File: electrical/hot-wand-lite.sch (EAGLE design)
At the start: 77 parts, among them IC1 12V R-78K12-2.0, IC2 AMS1117-5.0, Q1 NCHAN, Q2 SIRS5800DP-T1-GE3, Q3 DMTH64M2LPDWQ-13, Q4 2N7002K, Q5 G3404, U1 SEEED-XIAO-SAMD21, U2 1EDN8511BXUSA1, U3 LM74700QDBVTQ1, U4 AP53781

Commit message: added a selector for ISEL
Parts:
- removed JP4: (no value), hot-wand:M03LOCK
- removed SJ2: SOLDERJUMPERNO, hot-wand:SOLDERJUMPERNO
- JP5: device hot-wand:M03LOCK -> hot-wand:M06LOCK; JLC-DNP 1 -> (none)
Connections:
- removed net N$55: R15.2, SJ2.1
- removed net N$9: JP5.1, R18.2
- removed net SWDIO: JP4.2, R7.1, R8.1
- new net FAN-CTRL: JP5.2, R7.1, R8.1
- new net USB-I-SEL: JP5.5, R15.2
- new net USB-V-SEL: JP5.3, R18.2
- net +12V: now also JP5.1; no longer JP4.3
- net GND: now also JP5.4, JP5.6; no longer JP4.1, JP5.2, JP5.3, SJ2.2
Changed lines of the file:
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@@
-<attribute name="JLC-DNP" value="1"/>
-</part>
-<part name="SJ2" library="hot-wand" deviceset="SOLDERJUMPER" device="NO" value="">
 <attribute name="JLC-DNP" value="1"/>
 </part>
@@
 </part>
 <part name="U$2" library="hot-wand" deviceset="5V" device=""/>
-<part name="P+2" library="hot-wand" deviceset="+12V" device=""/>
 <part name="GND8" library="hot-wand" deviceset="GND" device=""/>
-<part name="JP5" library="hot-wand" deviceset="M03" device="LOCK">
-<attribute name="JLC-DNP" value="1"/>
-</part>
-<part name="GND9" library="hot-wand" deviceset="GND" device=""/>
 <part name="R17" library="hot-wand" deviceset="RESISTOR" device="0603-RES" value="3K">
 <attribute name="JLCPARTNUM" value="C4211"/>
 </part>
-<part name="GND10" library="hot-wand" deviceset="GND" device=""/>
 <part name="JP6" library="hot-wand" deviceset="M04" device="LOCK">
-<attribute name="JLC-DNP" value="1"/>
-</part>
-<part name="JP4" library="hot-wand" deviceset="M03" device="LOCK">
 <attribute name="JLC-DNP" value="1"/>
 </part>
@@
 <attribute name="JLC-DNP" value="1"/>
 </part>
-<part name="GND12" library="hot-wand" deviceset="GND" device=""/>
 <part name="PCB2" library="hot-wand" deviceset="PCB-ART-VER-LITE" device="">
 <attribute name="DNP" value="1"/>
@@
 <attribute name="JLCPARTNUM" value="C23242"/>
 </part>
+<part name="JP5" library="hot-wand" deviceset="M06" device="LOCK"/>
 </parts>
 <sheets>
@@
 <attribute name="VALUE" x="148.59" y="-567.436" size="1.778" layer="96"/>
 </instance>
-<instance part="SJ2" gate="1" x="165.1" y="-568.96"/>
 <instance part="R13" gate="G$1" x="157.48" y="-538.48" smashed="yes" rot="R270">
 <attribute name="NAME" x="153.8986" y="-534.67" size="1.778" layer="95" rot="R270"/>
@@
 </instance>
 <instance part="U$2" gate="G$1" x="109.22" y="-312.42"/>
-<instance part="P+2" gate="1" x="167.64" y="-398.78"/>
 <instance part="GND8" gate="1" x="109.22" y="-345.44"/>
-<instance part="JP5" gate="G$1" x="187.96" y="-609.6" rot="R180">
-<attribute name="JLC-DNP" x="187.96" y="-609.6" size="1.778" layer="96" rot="R180" display="off"/>
-</instance>
-<instance part="GND9" gate="1" x="172.72" y="-574.04"/>
 <instance part="R17" gate="G$1" x="172.72" y="-586.74" smashed="yes" rot="R270">
 <attribute name="NAME" x="169.1386" y="-582.93" size="1.778" layer="95" rot="R270"/>
@@
 <attribute name="JLCPARTNUM" x="172.72" y="-586.74" size="1.778" layer="96" rot="R270" display="off"/>
 </instance>
-<instance part="GND10" gate="1" x="177.8" y="-617.22"/>
 <instance part="JP6" gate="G$1" x="144.78" y="-317.5" rot="R180">
 <attribute name="JLC-DNP" x="144.78" y="-317.5" size="1.778" layer="96" rot="R180" display="off"/>
-</instance>
-<instance part="JP4" gate="G$1" x="147.32" y="-408.94">
-<attribute name="JLC-DNP" x="147.32" y="-408.94" size="1.778" layer="96" display="off"/>
 </instance>
 <instance part="GND11" gate="1" x="170.18" y="-190.5"/>
@@
 <attribute name="NAME" x="173.736" y="-334.772" size="1.778" layer="95" rot="R90"/>
 </instance>
-<instance part="GND12" gate="1" x="157.48" y="-416.56"/>
 <instance part="PCB2" gate="A" x="45.72" y="-132.08">
 <attribute name="JLC-DNP" x="45.72" y="-132.08" size="1.778" layer="96" display="off"/>
@@
 <attribute name="JLCPARTNUM" x="172.72" y="-599.44" size="1.778" layer="96" rot="R270" display="off"/>
 </instance>
+<instance part="JP5" gate="G$1" x="213.36" y="-584.2" rot="R180"/>
 </instances>
 <busses>
@@
 </segment>
 <segment>
-<pinref part="SJ2" gate="1" pin="2"/>
-<wire x1="172.72" y1="-568.96" x2="170.18" y2="-568.96" width="0.1524" layer="91"/>
-<pinref part="GND9" gate="1" pin="GND"/>
-<wire x1="172.72" y1="-571.5" x2="172.72" y2="-568.96" width="0.1524" layer="91"/>
-</segment>
-<segment>
-<pinref part="JP5" gate="G$1" pin="2"/>
-<pinref part="GND10" gate="1" pin="GND"/>
-<wire x1="180.34" y1="-609.6" x2="177.8" y2="-609.6" width="0.1524" layer="91"/>
-<wire x1="177.8" y1="-609.6" x2="177.8" y2="-612.14" width="0.1524" layer="91"/>
-<pinref part="JP5" gate="G$1" pin="3"/>
-<wire x1="177.8" y1="-612.14" x2="177.8" y2="-614.68" width="0.1524" layer="91"/>
-<wire x1="180.34" y1="-612.14" x2="177.8" y2="-612.14" width="0.1524" layer="91"/>
-<junction x="177.8" y="-612.14"/>
-</segment>
-<segment>
 <pinref part="JP1" gate="G$1" pin="2"/>
 <pinref part="GND11" gate="1" pin="GND"/>
 <wire x1="180.34" y1="-182.88" x2="170.18" y2="-182.88" width="0.1524" layer="91"/>
 <wire x1="170.18" y1="-182.88" x2="170.18" y2="-187.96" width="0.1524" layer="91"/>
-</segment>
-<segment>
-<pinref part="JP4" gate="G$1" pin="1"/>
-<pinref part="GND12" gate="1" pin="GND"/>
-<wire x1="154.94" y1="-411.48" x2="157.48" y2="-411.48" width="0.1524" layer="91"/>
-<wire x1="157.48" y1="-411.48" x2="157.48" y2="-414.02" width="0.1524" layer="91"/>
 </segment>
 <segment>
@@
 <junction x="203.2" y="-340.36"/>
 </segment>
+<segment>
+<pinref part="JP5" gate="G$1" pin="4"/>
+<wire x1="208.28" y1="-586.74" x2="203.2" y2="-586.74" width="0.1524" layer="91"/>
+<label x="203.2" y="-586.74" size="1.27" layer="95" rot="R180" xref="yes"/>
+</segment>
+<segment>
+<pinref part="JP5" gate="G$1" pin="6"/>
+<wire x1="208.28" y1="-591.82" x2="203.2" y2="-591.82" width="0.1524" layer="91"/>
+<label x="203.2" y="-591.82" size="1.27" layer="95" rot="R180" xref="yes"/>
+</segment>
 </net>
 <net name="+24V" class="0">
@@
 <pinref part="C12" gate="G$1" pin="+"/>
 <wire x1="193.04" y1="-497.84" x2="193.04" y2="-495.3" width="0.1524" layer="91"/>
+<junction x="193.04" y="-495.3"/>
 </segment>
 <segment>
@@
 </segment>
 <segment>
-<pinref part="P+2" gate="1" pin="+12V"/>
-<wire x1="154.94" y1="-406.4" x2="167.64" y2="-406.4" width="0.1524" layer="91"/>
-<wire x1="167.64" y1="-406.4" x2="167.64" y2="-401.32" width="0.1524" layer="91"/>
-<pinref part="JP4" gate="G$1" pin="3"/>
+<pinref part="JP5" gate="G$1" pin="1"/>
+<wire x1="208.28" y1="-579.12" x2="203.2" y2="-579.12" width="0.1524" layer="91"/>
+<label x="203.2" y="-579.12" size="1.27" layer="95" rot="R180" xref="yes"/>
 </segment>
 </net>
@@
 </segment>
 </net>
-<net name="SWDIO" class="0">
+<net name="FAN-CTRL" class="0">
 <segment>
 <pinref part="R7" gate="G$1" pin="1"/>
@@
 <pinref part="R8" gate="G$1" pin="1"/>
 <wire x1="170.18" y1="-408.94" x2="172.72" y2="-408.94" width="0.1524" layer="91"/>
-<wire x1="170.18" y1="-408.94" x2="154.94" y2="-408.94" width="0.1524" layer="91"/>
+<wire x1="170.18" y1="-408.94" x2="165.1" y2="-408.94" width="0.1524" layer="91"/>
 <junction x="170.18" y="-408.94"/>
-<pinref part="JP4" gate="G$1" pin="2"/>
+<label x="165.1" y="-408.94" size="1.27" layer="95" rot="R180" xref="yes"/>
+</segment>
+<segment>
+<pinref part="JP5" gate="G$1" pin="2"/>
+<wire x1="208.28" y1="-581.66" x2="203.2" y2="-581.66" width="0.1524" layer="91"/>
+<label x="203.2" y="-581.66" size="1.27" layer="95" rot="R180" xref="yes"/>
 </segment>
 </net>
@@
 <pinref part="R15" gate="G$1" pin="1"/>
 <wire x1="139.7" y1="-568.96" x2="147.32" y2="-568.96" width="0.1524" layer="91"/>
-</segment>
-</net>
-<net name="N$55" class="0">
-<segment>
-<pinref part="R15" gate="G$1" pin="2"/>
-<pinref part="SJ2" gate="1" pin="1"/>
-<wire x1="157.48" y1="-568.96" x2="160.02" y2="-568.96" width="0.1524" layer="91"/>
 </segment>
 </net>
@@
 </segment>
 </net>
-<net name="N$9" class="0">
-<segment>
-<pinref part="JP5" gate="G$1" pin="1"/>
+<net name="USB-V-SEL" class="0">
+<segment>
 <wire x1="172.72" y1="-607.06" x2="180.34" y2="-607.06" width="0.1524" layer="91"/>
 <pinref part="R18" gate="G$1" pin="2"/>
 <wire x1="172.72" y1="-607.06" x2="172.72" y2="-604.52" width="0.1524" layer="91"/>
+<label x="180.34" y="-607.06" size="1.27" layer="95" xref="yes"/>
+</segment>
+<segment>
+<pinref part="JP5" gate="G$1" pin="3"/>
+<wire x1="208.28" y1="-584.2" x2="203.2" y2="-584.2" width="0.1524" layer="91"/>
+<label x="203.2" y="-584.2" size="1.27" layer="95" rot="R180" xref="yes"/>
 </segment>
 </net>
@@
 </segment>
 </net>
+<net name="USB-I-SEL" class="0">
+<segment>
+<pinref part="JP5" gate="G$1" pin="5"/>
+<wire x1="208.28" y1="-589.28" x2="203.2" y2="-589.28" width="0.1524" layer="91"/>
+<label x="203.2" y="-589.28" size="1.27" layer="95" rot="R180" xref="yes"/>
+</segment>
+<segment>
+<pinref part="R15" gate="G$1" pin="2"/>
+<wire x1="157.48" y1="-568.96" x2="160.02" y2="-568.96" width="0.1524" layer="91"/>
+<label x="160.02" y="-568.96" size="1.27" layer="95" xref="yes"/>
+</segment>
+</net>

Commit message: documentation
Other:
- note added: "Kool Mu 0077932A7 22 AWG 19 ± 1 turns"
- note added: "Kool Mu 0077932A7 22 AWG 23 ± 1 turns"
- note added: "Kool Mu 0077932A7 22 AWG if 2 cores 9 or 10 turns if 1 core 18 to 20 turns"
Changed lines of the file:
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@@
 both SAMD21 and RP2040</text>
 <text x="73.66" y="-381" size="1.016" layer="97" rot="R180" align="top-left">(sub: 7812 eqv)</text>
+<text x="68.58" y="-182.88" size="0.6096" layer="97" align="top-left">Kool Mu 0077932A7
+22 AWG
+if 2 cores
+9 or 10 turns
+if 1 core
+18 to 20 turns</text>
+<text x="106.68" y="-182.88" size="0.6096" layer="97" align="top-left">Kool Mu 0077932A7
+22 AWG
+23 ± 1 turns</text>
+<text x="152.4" y="-195.58" size="0.6096" layer="97" align="top-left">Kool Mu 0077932A7
+22 AWG
+19 ± 1 turns</text>
 </plain>
 <instances>

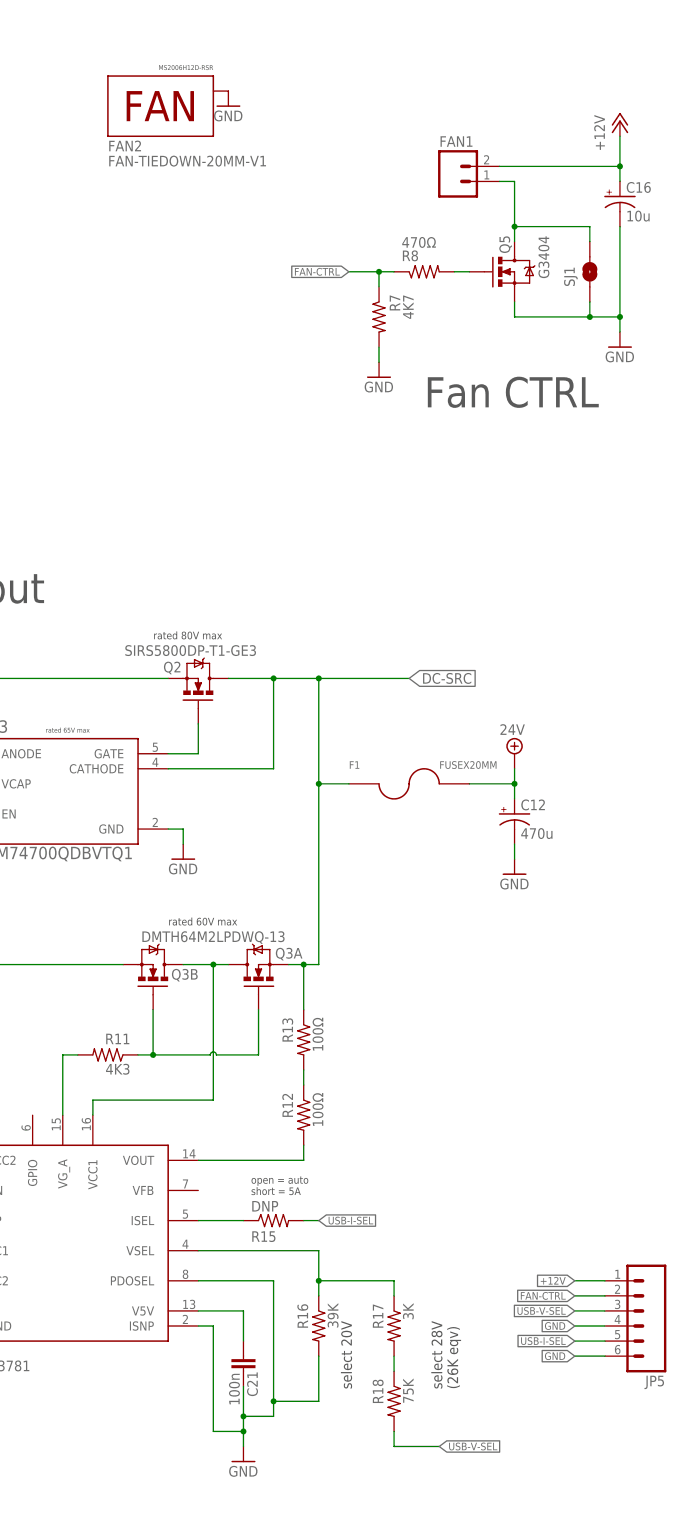
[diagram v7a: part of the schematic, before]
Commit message: lite, major design change, now 15V or 20V, 3A or 5A, no mosfet for fan
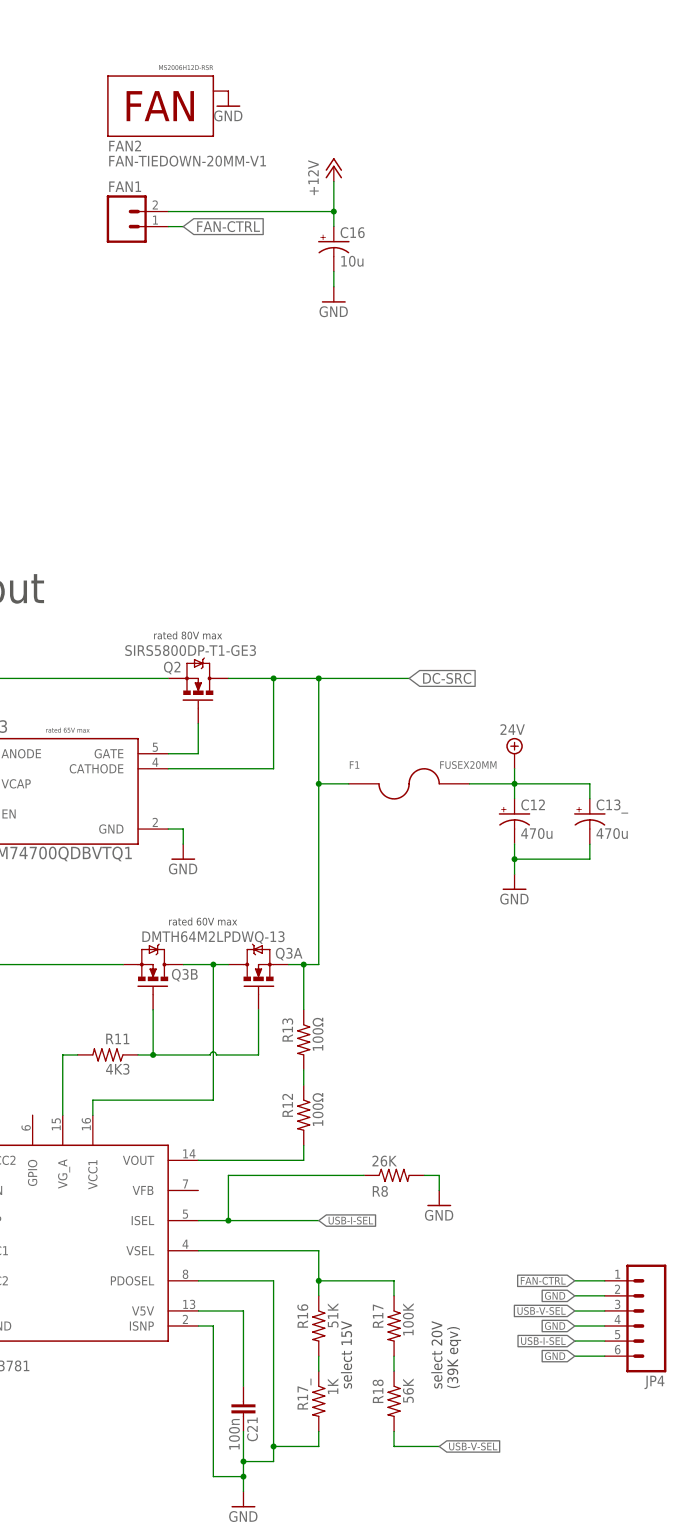
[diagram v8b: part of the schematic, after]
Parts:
- removed Q5: G3404, hot-wand:MOSFET-NCHANNELSMD
- removed R15: DNP, hot-wand:RESISTOR0603-RES
- removed R7: 4K7, hot-wand:RESISTOR0603-RES
- removed SJ1: SOLDERJUMPERNO, hot-wand:SOLDERJUMPERNO
- added C13_: 470u, hot-wand:CAP_POLPTH4
- added R17_: 1K, hot-wand:RESISTOR0603-RES
- R16: value 39K -> 51K; JLCPARTNUM C23153 -> ?
- R17: value 3K -> 100K
- R18: value 75K -> 56K
- R8: value 470Ω -> 26K; JLCPARTNUM C23179 -> ?
- renumbered JP5 to JP4
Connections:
- removed net N$52: FAN1.1, Q5.D, SJ1.2
- removed net N$53: Q5.G, R8.2
- removed net N$54: R15.1, U4.ISEL
- new net N$9: R16.2, R17_.1
- net +12V: no longer JP4.1
- net +24V: now also C13_.+
- net FAN-CTRL: now also FAN1.1, JP4.1; no longer JP4.2, R7.1, R8.1
- net GND: now also C13_.-, JP4.2, R17_.2, R8.2; no longer Q5.S, R16.2, R7.2, SJ1.1
- net USB-I-SEL: now also R8.1, U4.ISEL; no longer R15.2
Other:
- note added: "select 15V"
- note added: "select 20V (39K eqv)"
- note removed: "Fan CTRL"
- note removed: "open = auto short = 5A"
- note removed: "select 20V"
- note removed: "select 28V (26K eqv)"
- moved on the sheet: C16, C21, FAN1, R8
